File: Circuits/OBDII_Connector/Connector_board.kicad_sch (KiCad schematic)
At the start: 30 parts, among them J2 USB_C_Receptacle_USB2.0_14P, J4 Conn_02x08_Top_Bottom, J5 Conn_02x07_Counter_Clockwise, Q1 2N7002, Q2 MMDT3904, U1 TCAN3404, U2 ESP32-S3-WROOM-1, U3 AP2112K-3.3, U5 LM5164DDA, U7 CP2102N-Axx-xQFN24

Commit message: Full redesign of connector board, including removal of USB flashing. This is now done by the flasher board.
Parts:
- removed J2: USB_C_Receptacle_USB2.0_14P, Connector_USB:USB_C_Receptacle_Amphenol_12401948E412A, symbol Connector:USB_C_Receptacle_USB2.0_14P
- removed J4: Conn_02x08_Top_Bottom, Connector_PinSocket_2.54mm:PinSocket_2x08_P2.54mm_Vertical, symbol Connector_Generic:Conn_02x08_Top_Bottom
- removed J5: Conn_02x07_Counter_Clockwise, Connector_PinHeader_2.54mm:PinHeader_2x07_P2.54mm_Vertical, symbol Connector_Generic:Conn_02x07_Counter_Clockwise
- removed Q2: MMDT3904, Package_TO_SOT_SMD:SOT-363_SC-70-6, symbol Transistor_BJT:MMDT3904
- removed R10, R8, R9: 1k, Resistor_SMD:R_0603_1608Metric_Pad0.98x0.95mm_HandSolder, symbol Device:R
- removed R11: 22k, Resistor_SMD:R_0603_1608Metric_Pad0.98x0.95mm_HandSolder, symbol Device:R
- removed R12: 47k, Resistor_SMD:R_0603_1608Metric_Pad0.98x0.95mm_HandSolder, symbol Device:R
- removed R13, R14: 5.1k, Resistor_SMD:R_0603_1608Metric_Pad0.98x0.95mm_HandSolder, symbol Device:R
- removed R17: 10k, Resistor_SMD:R_0603_1608Metric_Pad0.98x0.95mm_HandSolder, symbol Device:R
- removed U7: CP2102N-Axx-xQFN24, Package_DFN_QFN:QFN-24-1EP_4x4mm_P0.5mm_EP2.6x2.6mm, symbol Interface_USB:CP2102N-Axx-xQFN24
- added C4: 1uF, Capacitor_SMD:C_0805_2012Metric_Pad1.18x1.45mm_HandSolder, symbol Device:C
- added C5: 4.7uF, Capacitor_SMD:C_0805_2012Metric_Pad1.18x1.45mm_HandSolder, symbol Device:C
- added C7: 0.1uF, Capacitor_SMD:C_0805_2012Metric_Pad1.18x1.45mm_HandSolder, symbol Device:C
- added J1: Conn_01x06_Pin, Connector_PinSocket_2.54mm:PinSocket_1x06_P2.54mm_Vertical, symbol Connector:Conn_01x06_Pin
- added J2: Conn_02x08_Top_Bottom, Connector_PinSocket_2.54mm:PinSocket_2x08_P2.54mm_Vertical, symbol Connector_Generic:Conn_02x08_Top_Bottom
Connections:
- net LCD_LED is gone; now on net TCAN3404_SHDN: U2.25 (IO48)
- net LCD_T_CLK is gone; now on net TCAN3404_STB: U2.26 (IO45)
- net +3.3V: now also R16.1, C4.1, C5.1
- net CAN_RXD: now also U2.24 (IO47); no longer U2.6 (IO6)
- net CAN_TXD: now also U2.23 (IO21); no longer U2.5 (IO5)
- net ESP_EN: now also R16.2, C7.1, J1.6 (Pin_6)
- net ESP_IO0: now also J1.5 (Pin_5); no longer R16.1
- net ESP_RX: now also J1.3 (Pin_3)
- net ESP_TX: now also J1.4 (Pin_4)
- net GND: now also C4.2, C5.2, C7.2, J1.2 (Pin_2), J2.5 (Pin_5); no longer R16.2
- net TCAN3404_SHDN: no longer U2.9 (IO16)
- net TCAN3404_STB: no longer U2.8 (IO15)
- net USB_VBUS: now also J1.1 (Pin_1)
- net at D3.2 (A): now also J2.16 (Pin_16)
- net CANH renamed CAN+
- net CAN+: now also J2.6 (Pin_6)
- net CANL renamed CAN-
- net CAN-: now also J2.14 (Pin_14)
- net LCD_CS: no longer names the net of U2.35 (IO42)
- net LCD_DC: no longer names the net of U2.34 (IO41)
- net LCD_MISO: no longer names the net of U2.32 (IO39)
- net LCD_MOSI: no longer names the net of U2.39 (IO1)
- net LCD_RESET: no longer names the net of U2.38 (IO2)
- net LCD_SCK: no longer names the net of U2.33 (IO40)
- net LCD_T_CS: no longer names the net of U2.31 (IO38)
- net LCD_T_DIN: no longer names the net of U2.28 (IO35)
- net LCD_T_DO: no longer names the net of U2.30 (IO37)
- net LCD_T_IRQ: no longer names the net of U2.29 (IO36)
- no-connect marks 24 -> 13
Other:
- note removed: "Figure 2.6 of datasheet Self-powered devices should have this divider from VBUS to protect it from something"

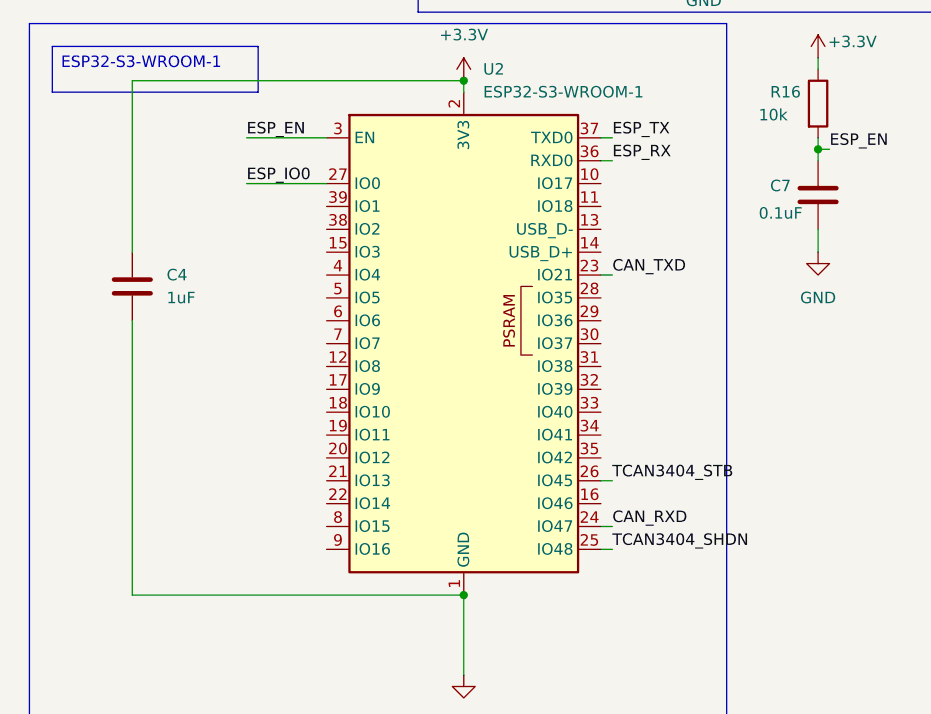
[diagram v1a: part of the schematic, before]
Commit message: Updated portside schematic
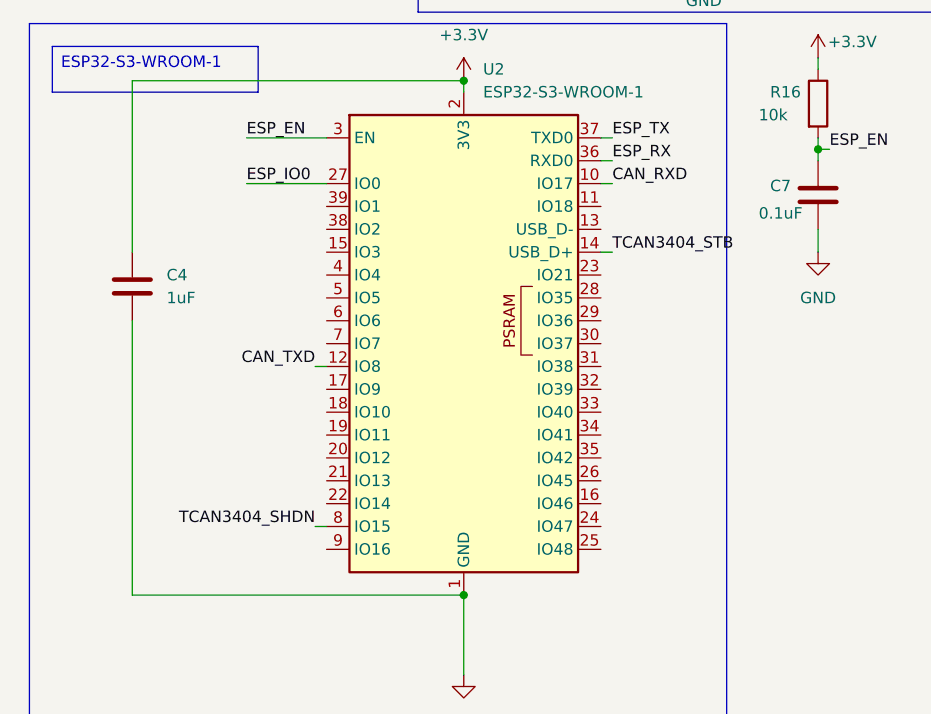
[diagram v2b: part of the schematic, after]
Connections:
- net CAN_RXD: now also U2.10 (IO17); no longer U2.24 (IO47)
- net CAN_TXD: now also U2.12 (IO8); no longer U2.23 (IO21)
- net TCAN3404_SHDN: now also U2.8 (IO15); no longer U2.25 (IO48)
- net TCAN3404_STB: now also U2.14 (USB_D+); no longer U2.26 (IO45)
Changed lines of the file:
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@@
+	(wire
+		(pts
+			(xy 45.72 148.59) (xy 46.99 148.59)
+		)
+		(stroke
+			(width 0)
+			(type default)
+		)
+	)
 	(wire
 		(pts
@@
 	(wire
 		(pts
+			(xy 77.47 128.27) (xy 78.74 128.27)
+		)
+		(stroke
+			(width 0)
+			(type default)
+		)
+	)
+	(wire
+		(pts
 			(xy 271.78 101.6) (xy 271.78 104.14)
 		)
@@
 	(wire
 		(pts
+			(xy 45.72 166.37) (xy 46.99 166.37)
+		)
+		(stroke
+			(width 0)
+			(type default)
+		)
+	)
+	(wire
+		(pts
 			(xy 266.7 114.3) (xy 271.78 114.3)
 		)
@@
 	(wire
 		(pts
+			(xy 77.47 135.89) (xy 78.74 135.89)
+		)
+		(stroke
+			(width 0)
+			(type default)
+		)
+	)
+	(wire
+		(pts
 			(xy 34.29 39.37) (xy 34.29 44.45)
 		)
@@
 	(wire
 		(pts
-			(xy 77.47 138.43) (xy 78.74 138.43)
-		)
-		(stroke
-			(width 0)
-			(type default)
-		)
-	)
-	(wire
-		(pts
 			(xy 264.16 30.48) (xy 266.7 30.48)
 		)
@@
 	(wire
 		(pts
-			(xy 77.47 161.29) (xy 78.74 161.29)
-		)
-		(stroke
-			(width 0)
-			(type default)
-		)
-	)
-	(wire
-		(pts
 			(xy 68.58 20.32) (xy 76.2 20.32)
 		)
@@
 	(wire
 		(pts
-			(xy 77.47 168.91) (xy 78.74 168.91)
-		)
-		(stroke
-			(width 0)
-			(type default)
-		)
-	)
-	(wire
-		(pts
 			(xy 99.06 52.07) (xy 49.53 52.07)
 		)
@@
 		(pts
 			(xy 77.47 125.73) (xy 78.74 125.73)
-		)
-		(stroke
-			(width 0)
-			(type default)
-		)
-	)
-	(wire
-		(pts
-			(xy 77.47 166.37) (xy 78.74 166.37)
 		)
 		(stroke
@@
 	)
 	(label "CAN_TXD"
-		(at 78.74 138.43 0)
-		(effects
-			(font
-				(size 1.27 1.27)
-			)
-			(justify left bottom)
+		(at 45.72 148.59 180)
+		(effects
+			(font
+				(size 1.27 1.27)
+			)
+			(justify right bottom)
 		)
 	)
@@
 	)
 	(label "TCAN3404_SHDN"
-		(at 78.74 168.91 0)
-		(effects
-			(font
-				(size 1.27 1.27)
-			)
-			(justify left bottom)
+		(at 45.72 166.37 180)
+		(effects
+			(font
+				(size 1.27 1.27)
+			)
+			(justify right bottom)
 		)
 	)
@@
 	)
 	(label "CAN_RXD"
-		(at 78.74 166.37 0)
+		(at 78.74 128.27 0)
 		(effects
 			(font
@@
 	)
 	(label "TCAN3404_STB"
-		(at 78.74 161.29 0)
-		(effects
-			(font
+		(at 78.74 135.89 0)
+		(effects
+			(font
